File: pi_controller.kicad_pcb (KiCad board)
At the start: 4 copper layers, 99.7 x 91.3 mm, 160 parts, among them J1 PWM, J2 DC Supply, J26 LED6, J27 LED5, J28 LED7, J29 LED8, J30 I2C, J31 UART, J32 LED3, J33 LED1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

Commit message: Project name change to signalbridge and board final revision
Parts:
- removed the G*** at (105.5, 84.5)
- added G***: LOGO, pi_controller:logo-signalbridge, B.Cu at (105.8, 85.5)
- AN1, AN10, AN11, AN12, AN13, AN14, AN15, AN16, AN2, AN3, AN4, AN5, AN6, AN7, AN8, AN9: footprint PiMatrix:JST_ZH_B3B-ZR_1x03_P1.50mm_Vertical_SilkSafe -> pi_controller:JST_ZH_B3B-ZR_1x03_P1.50mm_Vertical_SilkSafe
- J2: footprint Connector_BarrelJack:BarrelJack_Horizontal -> pi_controller:BarrelJack_Horizontal
- J26, J27, J28, J29, J32, J33, J34, J35, JR1, JR2, JR3, JR4, JR5, JR6, JR7, JR8: footprint Connector_PinHeader_2.54mm:PinHeader_2x08_P2.54mm_Vertical -> pi_controller:PinHeader_2x08_P2.54mm_Vertical
- J30, J31: footprint PiMatrix:JST_ZH_B4B-ZR_1x04_P1.50mm_Vertical_SilkSafe -> pi_controller:JST_ZH_B4B-ZR_1x04_P1.50mm_Vertical_SilkSafe
- JSPI1, JSPI2, JSPI3, JSPI4, JSPI5, JSPI6, JSPI7: footprint PiMatrix:JST_ZH_B6B-ZR_1x06_P1.50mm_Vertical_SilkSafe -> pi_controller:JST_ZH_B6B-ZR_1x06_P1.50mm_Vertical_SilkSafe
- U4: footprint PiMatrix:RaspberryPi_Pico_Common_THT_CustomSilk -> pi_controller:RaspberryPi_Pico_Common_THT_CustomSilk
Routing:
- net VDDA: track 155.6 -> 154.1 mm
- net /SEG1: track 34.9 -> 33.8 mm
- net /SEG2: track 26.5 -> 26.0 mm
- net /SEG10: track 51.5 -> 51.0 mm
- net /ROW6: track 50.4 -> 49.9 mm

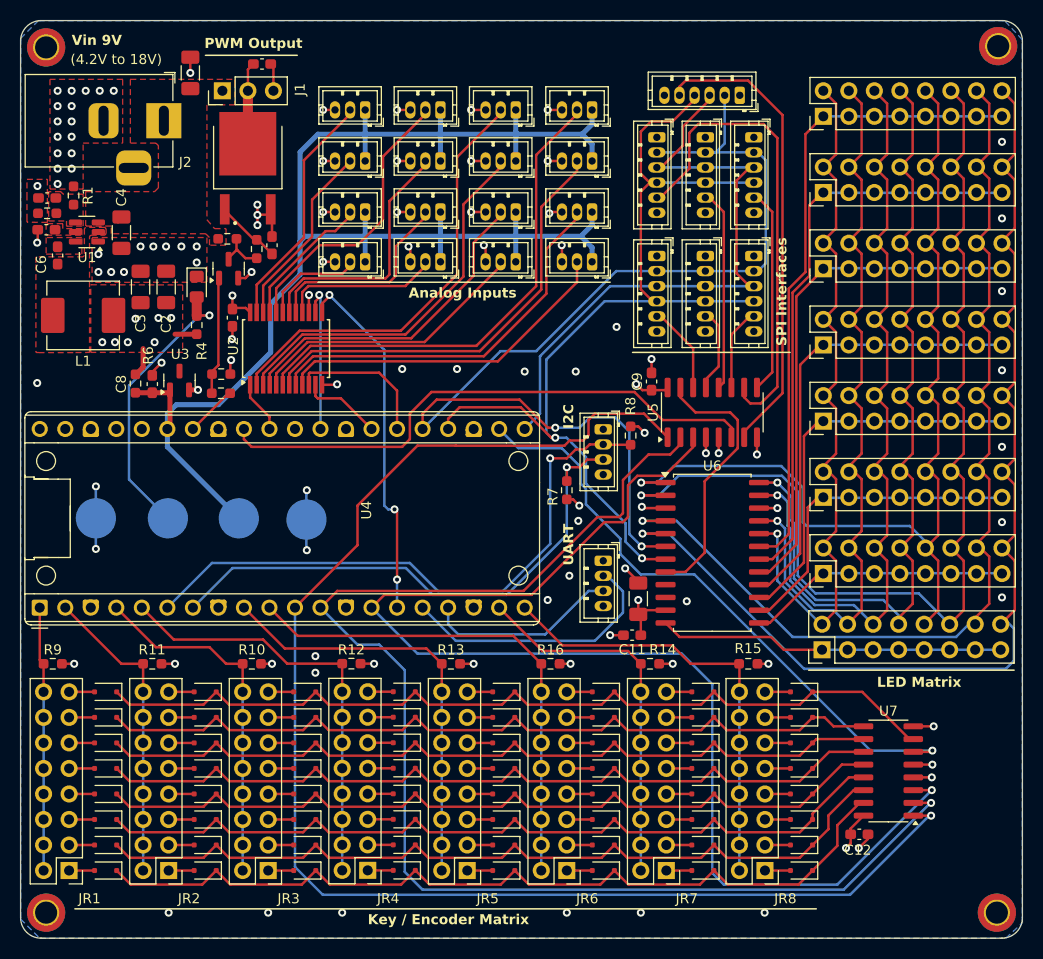
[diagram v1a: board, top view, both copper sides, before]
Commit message: Created the slot for the pi and udpated silk screen
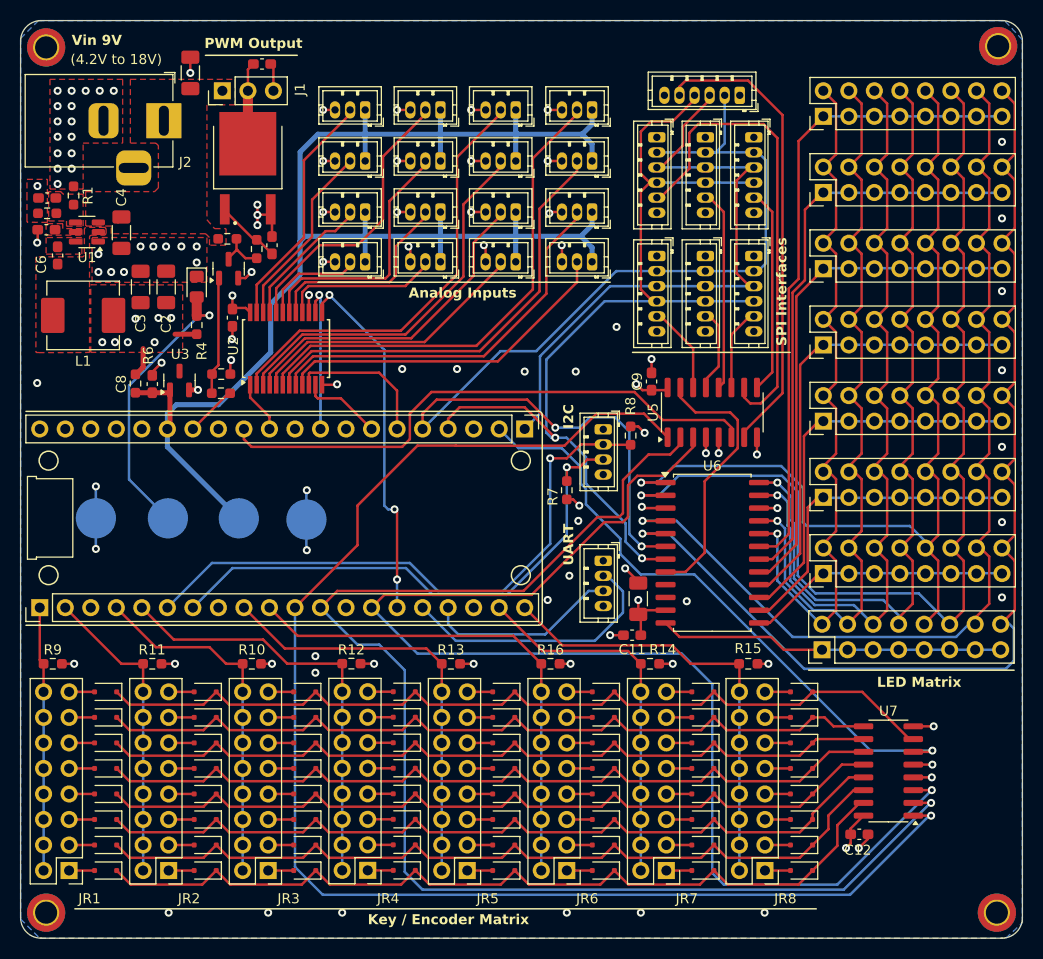
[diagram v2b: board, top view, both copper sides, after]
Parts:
- removed U4: RaspberryPi_Pico, pi_controller:RaspberryPi_Pico_Common_THT_CustomSilk
- added J3: Conn_01x20, Connector_PinHeader_2.54mm:PinHeader_1x20_P2.54mm_Vertical, F.Cu at (91.1, 114.6)
- added J4: Conn_01x20, Connector_PinHeader_2.54mm:PinHeader_1x20_P2.54mm_Vertical, F.Cu at (139.3, 96.8)
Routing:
- net /COL_MUX_A: track 144.6 -> 143.7 mm

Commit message: Adjusting testpoint pads and adding 74hc4051 datasheet
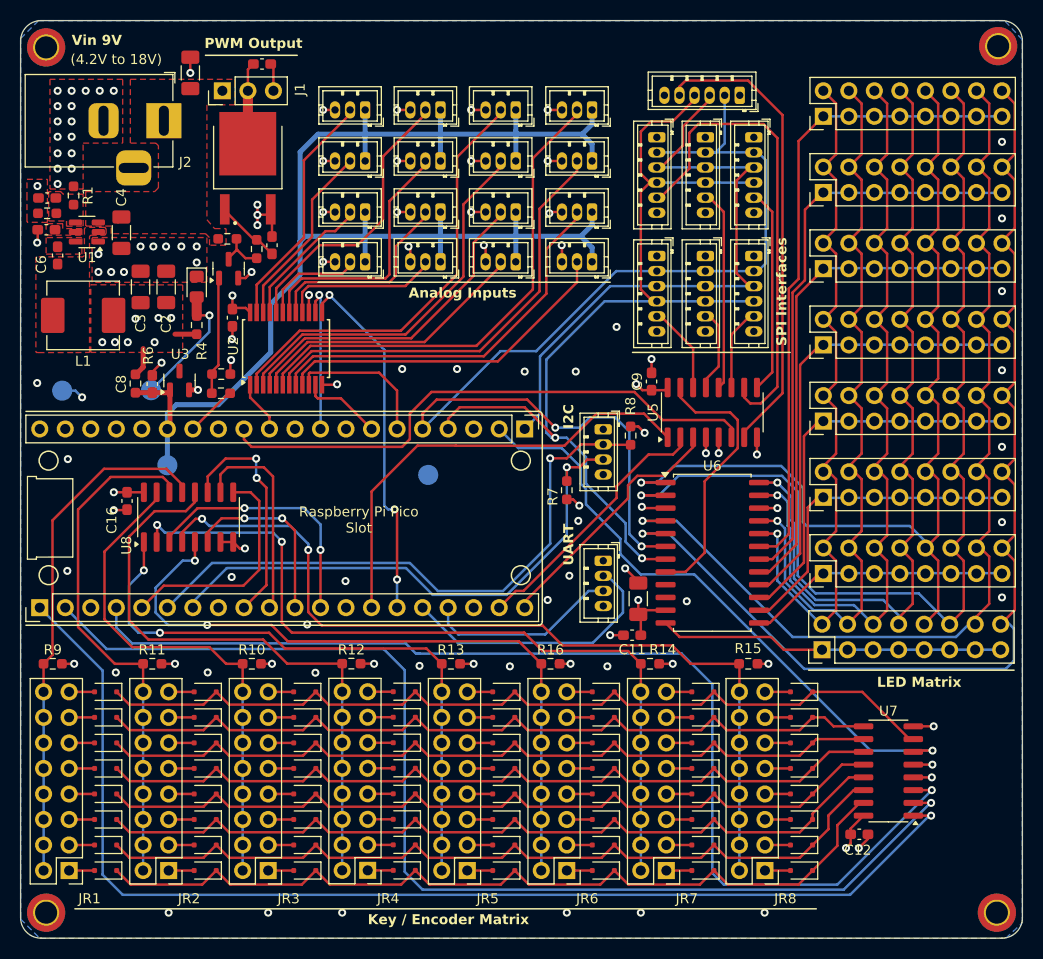
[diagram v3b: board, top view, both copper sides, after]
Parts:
- added C16: 0.1uF, Capacitor_SMD:C_0603_1608Metric_Pad1.08x0.95mm_HandSolder, F.Cu at (99.7, 103.9)
- added U8: CD74HC4051M96, Package_SO:SOIC-16_3.9x9.9mm_P1.27mm, F.Cu at (105.9, 105.5)
- TP1, TP2, TP3, TP4: footprint TestPoint:TestPoint_Pad_D4.0mm -> pi_controller:TestPoint_Pad_D2.0mm
- moved TP4 13.1 mm to (93.3, 93.0)
- moved TP1 12.9 mm to (129.7, 101.3)
- moved TP3 12.9 mm to (102.1, 92.9)
- moved TP2 8.86 mm to (103.8, 100.4)
- moved G*** 3.12 mm to (104.1, 82.9)
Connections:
- net /CS_KEY renamed /CS_COL
- net /CS_LED renamed /SPI_MUX_CS
- J3 pad 1: /ROW1 -> /COL_MUX_A
- J3 pad 10: /ROW6 -> /ROW_MUX_B
- J3 pad 11: /COL_MUX_A -> /CS_ROW
- J3 pad 12: /COL_MUX_B -> /ROW_INPUT
- J3 pad 14: /COL_MUX_C -> /SPI_MUX_A
- J3 pad 19: /ROW7 -> /SPI_MUX_B
- J3 pad 2: /ROW2 -> /COL_MUX_B
- J3 pad 20: /ROW8 -> /SPI_MUX_C
- J3 pad 4: /ROW3 -> /COL_MUX_C
- J3 pad 5: /ROW4 -> /ROW_MUX_C
- J3 pad 9: /ROW5 -> /ROW_MUX_A
- U5 pad 1: /COL_MUX_A -> /SPI_MUX_A
- U5 pad 2: /COL_MUX_B -> /SPI_MUX_B
- U5 pad 3: /COL_MUX_C -> /SPI_MUX_C
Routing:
- net /SPI_MUX_A: track 0.00 -> 45.2 mm
- net /ROW7: track 37.0 -> 80.8 mm, vias 0 -> 2
- net /ROW8: track 44.2 -> 87.2 mm, vias 0 -> 2
- net /SPI_MUX_B: track 0.00 -> 26.3 mm
- net /COL_MUX_A: track 143.7 -> 117.5 mm
- net /ROW_INPUT: track 0.00 -> 25.2 mm, vias 0 -> 2
- net /SPI_MUX_C: track 0.00 -> 24.9 mm
- net /ROW1: track 26.3 -> 50.9 mm
- net /ROW_MUX_A: track 0.00 -> 23.3 mm, vias 0 -> 2
- net /ROW_MUX_C: track 0.00 -> 23.0 mm
- net /ROW2: track 30.6 -> 51.8 mm
- net /ROW6: track 49.9 -> 70.4 mm, vias 0 -> 2
- net /ROW_MUX_B: track 0.00 -> 20.4 mm
- net /COL_MUX_B: track 134.7 -> 115.0 mm
- net /ROW5: track 42.6 -> 62.1 mm, vias 0 -> 2
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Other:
- board text added: "Raspberry Pi Pico Slot"

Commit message: Upgrading power supply protection
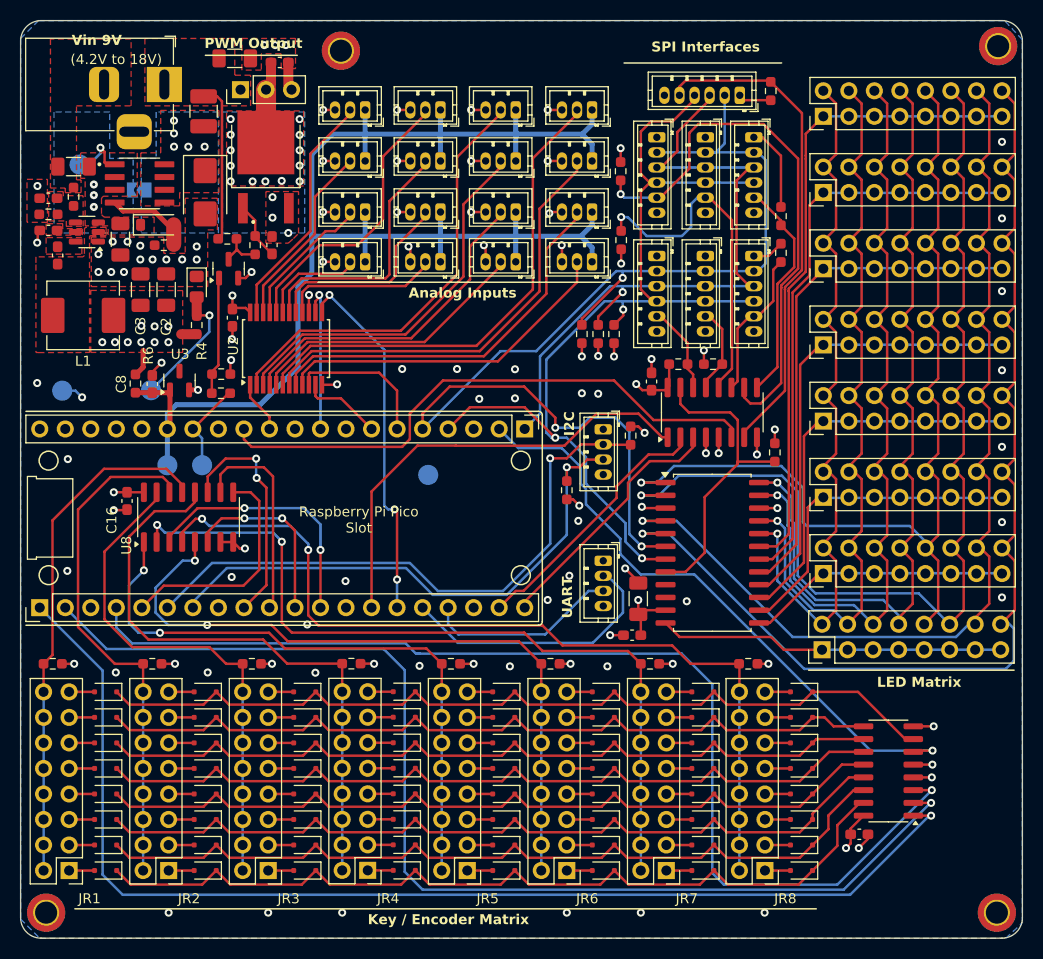
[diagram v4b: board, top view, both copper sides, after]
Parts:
- added C17: 22uF, Capacitor_SMD:C_1206_3216Metric_Pad1.33x1.80mm_HandSolder, F.Cu at (94.4, 70.7)
- added D66: Z2SMBJ18A, Diode_SMD:D_SMB, F.Cu at (107.5, 73.2)
- added D67: BZT52C12, Diode_SMD:D_SOD-123, F.Cu at (102.7, 76.5)
- added F1: Polyfuse, Fuse:Fuse_1210_3225Metric_Pad1.42x2.65mm_HandSolder, F.Cu at (107.4, 65.2)
- added JP1: Jumper_2_Open, Jumper:SolderJumper-2_P1.3mm_Open_TrianglePad1.0x1.5mm, B.Cu at (101.0, 73.0)
- added Q3: AO4407A, AO4407A:SOIC127P600X175-8N, F.Cu at (101.0, 72.3)
- added R19: 4.7k, Resistor_SMD:R_0603_1608Metric_Pad0.98x0.95mm_HandSolder, F.Cu at (164.2, 99.1)
- added R20: 4.7k, Resistor_SMD:R_0603_1608Metric_Pad0.98x0.95mm_HandSolder, F.Cu at (154.6, 90.3)
- added R21: 4.7k, Resistor_SMD:R_0603_1608Metric_Pad0.98x0.95mm_HandSolder, F.Cu at (158.1, 90.3)
- added R22: 4.7k, Resistor_SMD:R_0603_1608Metric_Pad0.98x0.95mm_HandSolder, F.Cu at (148.9, 78.0)
- added R23: 4.7k, Resistor_SMD:R_0603_1608Metric_Pad0.98x0.95mm_HandSolder, F.Cu at (164.8, 79.2)
- added R24: 4.7k, Resistor_SMD:R_0603_1608Metric_Pad0.98x0.95mm_HandSolder, F.Cu at (148.9, 71.1)
- added R25: 4.7k, Resistor_SMD:R_0603_1608Metric_Pad0.98x0.95mm_HandSolder, F.Cu at (164.8, 75.6)
- added R26: 4.7k, Resistor_SMD:R_0603_1608Metric_Pad0.98x0.95mm_HandSolder, F.Cu at (163.8, 63.1)
- added R27: 4.7k, Resistor_SMD:R_0603_1608Metric_Pad0.98x0.95mm_HandSolder, F.Cu at (145.0, 87.3)
- added R28: 4.7k, Resistor_SMD:R_0603_1608Metric_Pad0.98x0.95mm_HandSolder, F.Cu at (146.6, 87.3)
- added R29: 4.7k, Resistor_SMD:R_0603_1608Metric_Pad0.98x0.95mm_HandSolder, F.Cu at (148.2, 87.3)
- added R30: 10k, Resistor_SMD:R_0603_1608Metric_Pad0.98x0.95mm_HandSolder, F.Cu at (103.4, 78.5)
- added TP5: TestPoint, pi_controller:TestPoint_Pad_D2.0mm, B.Cu at (107.2, 100.4)
- added TP6: TestPoint, pi_controller:TestPoint_Pad_D2.0mm, B.Cu at (95.0, 70.5)
- moved G*** 57.8 mm to (157.5, 105.0), turned to -90 degrees
- moved H1 29.3 mm to (121.0, 59.1)
- moved C15 4.65 mm to (110.5, 59.9), turned to 0 degrees
- moved J2 3.61 mm to (103.5, 62.5)
- moved J1 1.81 mm to (111.0, 63.0)
- moved Q1 1.81 mm to (113.6, 70.7)
- moved C13 1.76 mm to (114.9, 60.3)
- moved C4 0.67 mm to (99.1, 77.9)
- moved R18 0.41 mm to (112.5, 78.5)
- moved C2 0.27 mm to (103.6, 82.9)
- moved C3 0.27 mm to (101.1, 82.9)
- moved C5 0.21 mm to (91.9, 77.0)
- moved R2 0.16 mm to (91.9, 75.4)
- moved C7 0.13 mm to (91.9, 73.8)
- moved R1 0.12 mm to (94.4, 73.7)
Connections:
- C4 pad 2: +9V -> Net-(D67-K)
- U1 pad 3: +9V -> Net-(D67-K)
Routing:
- net +3V3: track 40.0 -> 66.1 mm, vias 24 -> 33
- net +9V: track 0.77 -> 15.9 mm
- net /CS4: track 19.7 -> 33.8 mm, vias 0 -> 1
- net Net-(D67-A): track 0.00 -> 8.85 mm
- net /MOSI: track 107.9 -> 116.6 mm, vias 2 -> 3
- net /CS6: track 47.3 -> 54.2 mm, vias 0 -> 1
- net /CS5: track 7.84 -> 14.6 mm
- net GND: track 67.4 -> 60.9 mm, vias 102 -> 93
- net Net-(D67-K): track 0.00 -> 5.81 mm, vias 0 -> 4
- net /MISO: track 63.3 -> 68.2 mm, vias 0 -> 1
- net /CS1: track 26.9 -> 31.0 mm
- net /PWM_OUT: track 5.03 -> 9.01 mm
- net /CS8: track 45.9 -> 48.7 mm
- net /CS7: track 20.1 -> 22.3 mm
- net /SCLK: track 97.9 -> 100.0 mm, vias 2 -> 3
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- added copper zone on B.Cu, net Net-(D66-K)
- added copper zone on F.Cu, net Net-(D66-K)
- added copper zone on B.Cu, net Net-(D67-K)
- added copper zone on F.Cu, net Net-(D67-K)
- added copper zone on B.Cu, net Net-(J1-Pin_2)
- added copper zone on F.Cu, net Net-(J1-Pin_2)
